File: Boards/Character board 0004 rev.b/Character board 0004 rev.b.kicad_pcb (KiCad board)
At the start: 2 copper layers, 166.4 x 186.7 mm, 65 parts, among them J1 card edge, J2 character connector, Q1 2N6125, U1 2.2K, U10 Unused DIP, U11 ULN2003A, U12 ULN2003A, U13 7406, U14 74LS42, U15 LM741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

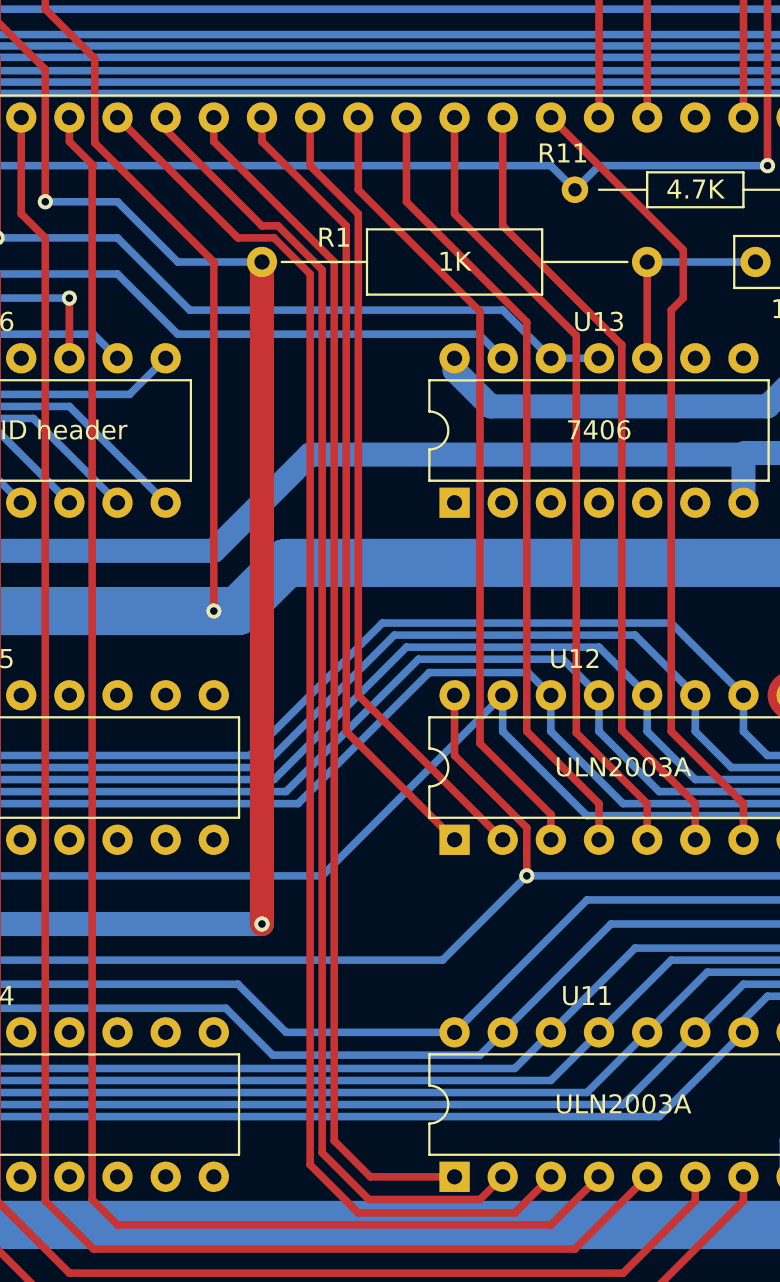
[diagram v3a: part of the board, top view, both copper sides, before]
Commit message: revisions from real life boards
tip130a is actually tip30a, widened holes for crystal, widened holes for big power resistor, fixed cpu board LED resistors
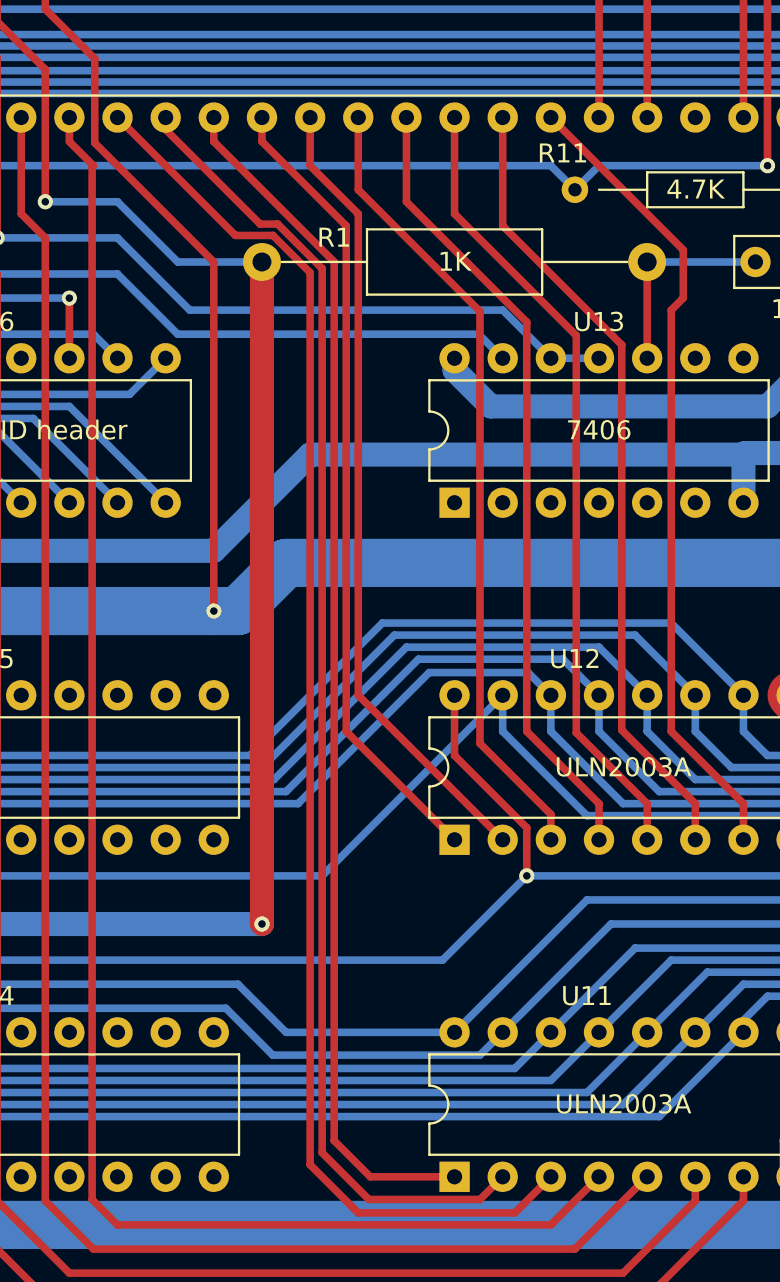
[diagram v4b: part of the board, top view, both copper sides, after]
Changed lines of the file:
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@@
     (fp_line (start 20.32 0) (end 14.66 0)
       (stroke (width 0.1) (type solid)) (layer "F.Fab"))
-    (pad "1" thru_hole circle (at 0 0) (size 1.6 1.6) (drill 0.8) (layers "*.Cu" "*.Mask")
+    (pad "1" thru_hole circle (at 0 0) (size 2 2) (drill 1) (layers "*.Cu" "*.Mask")
       (net 184 "24Vpu") (pintype "passive"))
-    (pad "2" thru_hole oval (at 20.32 0) (size 1.6 1.6) (drill 0.8) (layers "*.Cu" "*.Mask")
+    (pad "2" thru_hole circle (at 20.32 0) (size 2 2) (drill 1) (layers "*.Cu" "*.Mask")
       (net 182 "Net-(C11-Pad1)") (pintype "passive"))
     (model "${KICAD6_3DMODEL_DIR}/Resistor_THT.3dshapes/R_Axial_DIN0309_L9.0mm_D3.2mm_P20.32mm_Horizontal.wrl"
@@
   (segment (start 118.11 91.44) (end 118.04 91.51) (width 0.4) (layer "F.Cu") (net 170))
   (segment (start 116.84 90.17) (end 118.11 91.44) (width 0.4) (layer "F.Cu") (net 170))
-  (segment (start 119.38 88.9) (end 125.73 95.25) (width 0.4) (layer "F.Cu") (net 171))
-  (segment (start 125.73 95.25) (end 127.635 95.25) (width 0.4) (layer "F.Cu") (net 171))
-  (segment (start 132.08 146.685) (end 140.335 146.685) (width 0.4) (layer "F.Cu") (net 171))
+  (segment (start 127.579899 95.12) (end 129.54 97.080101) (width 0.4) (layer "F.Cu") (net 171))
+  (segment (start 119.38 88.9) (end 125.6 95.12) (width 0.4) (layer "F.Cu") (net 171))
+  (segment (start 129.54 97.080101) (end 129.54 144.145) (width 0.4) (layer "F.Cu") (net 171))
   (segment (start 140.335 146.685) (end 142.24 144.78) (width 0.4) (layer "F.Cu") (net 171))
+  (segment (start 132.08 146.685) (end 140.335 146.685) (width 0.4) (layer "F.Cu") (net 171))
   (segment (start 129.54 144.145) (end 132.08 146.685) (width 0.4) (layer "F.Cu") (net 171))
-  (segment (start 127.635 95.25) (end 129.54 97.155) (width 0.4) (layer "F.Cu") (net 171))
-  (segment (start 129.54 97.155) (end 129.54 144.145) (width 0.4) (layer "F.Cu") (net 171))
-  (segment (start 127.848528 94.615) (end 130.175 96.941472) (width 0.4) (layer "F.Cu") (net 172))
-  (segment (start 130.175 143.51) (end 132.645 145.98) (width 0.4) (layer "F.Cu") (net 172))
-  (segment (start 121.92 89.535) (end 127 94.615) (width 0.4) (layer "F.Cu") (net 172))
-  (segment (start 127 94.615) (end 127.848528 94.615) (width 0.4) (layer "F.Cu") (net 172))
-  (segment (start 130.175 96.941472) (end 130.175 143.51) (width 0.4) (layer "F.Cu") (net 172))
+  (segment (start 125.6 95.12) (end 127.579899 95.12) (width 0.4) (layer "F.Cu") (net 171))
+  (segment (start 132.645 145.98) (end 138.5 145.98) (width 0.4) (layer "F.Cu") (net 172))
+  (segment (start 126.905 94.52) (end 127.828427 94.52) (width 0.4) (layer "F.Cu") (net 172))
   (segment (start 121.92 88.9) (end 121.92 89.535) (width 0.4) (layer "F.Cu") (net 172))
+  (segment (start 130.175 96.866573) (end 130.175 143.51) (width 0.4) (layer "F.Cu") (net 172))
+  (segment (start 130.175 143.51) (end 132.645 145.98) (width 0.4) (layer "F.Cu") (net 172))
+  (segment (start 121.92 89.535) (end 126.905 94.52) (width 0.4) (layer "F.Cu") (net 172))
+  (segment (start 127.828427 94.52) (end 130.175 96.866573) (width 0.4) (layer "F.Cu") (net 172))
   (segment (start 138.5 145.98) (end 139.7 144.78) (width 0.4) (layer "F.Cu") (net 172))
-  (segment (start 132.645 145.98) (end 138.5 145.98) (width 0.4) (layer "F.Cu") (net 172))
-  (segment (start 124.46 90.17) (end 130.81 96.52) (width 0.4) (layer "F.Cu") (net 173))
+  (segment (start 130.81 142.875) (end 132.715 144.78) (width 0.4) (layer "F.Cu") (net 173))
+  (segment (start 132.715 144.78) (end 137.16 144.78) (width 0.4) (layer "F.Cu") (net 173))
   (segment (start 130.81 96.52) (end 130.81 142.875) (width 0.4) (layer "F.Cu") (net 173))
+  (segment (start 124.46 90.17) (end 130.81 96.52) (width 0.4) (layer "F.Cu") (net 173))
   (segment (start 124.46 88.9) (end 124.46 90.17) (width 0.4) (layer "F.Cu") (net 173))
-  (segment (start 132.715 144.78) (end 137.16 144.78) (width 0.4) (layer "F.Cu") (net 173))
-  (segment (start 130.81 142.875) (end 132.715 144.78) (width 0.4) (layer "F.Cu") (net 173))
   (segment (start 131.445 94.615) (end 131.445 121.285) (width 0.4) (layer "F.Cu") (net 174))
   (segment (start 127 88.9) (end 127 90.17) (width 0.4) (layer "F.Cu") (net 174))

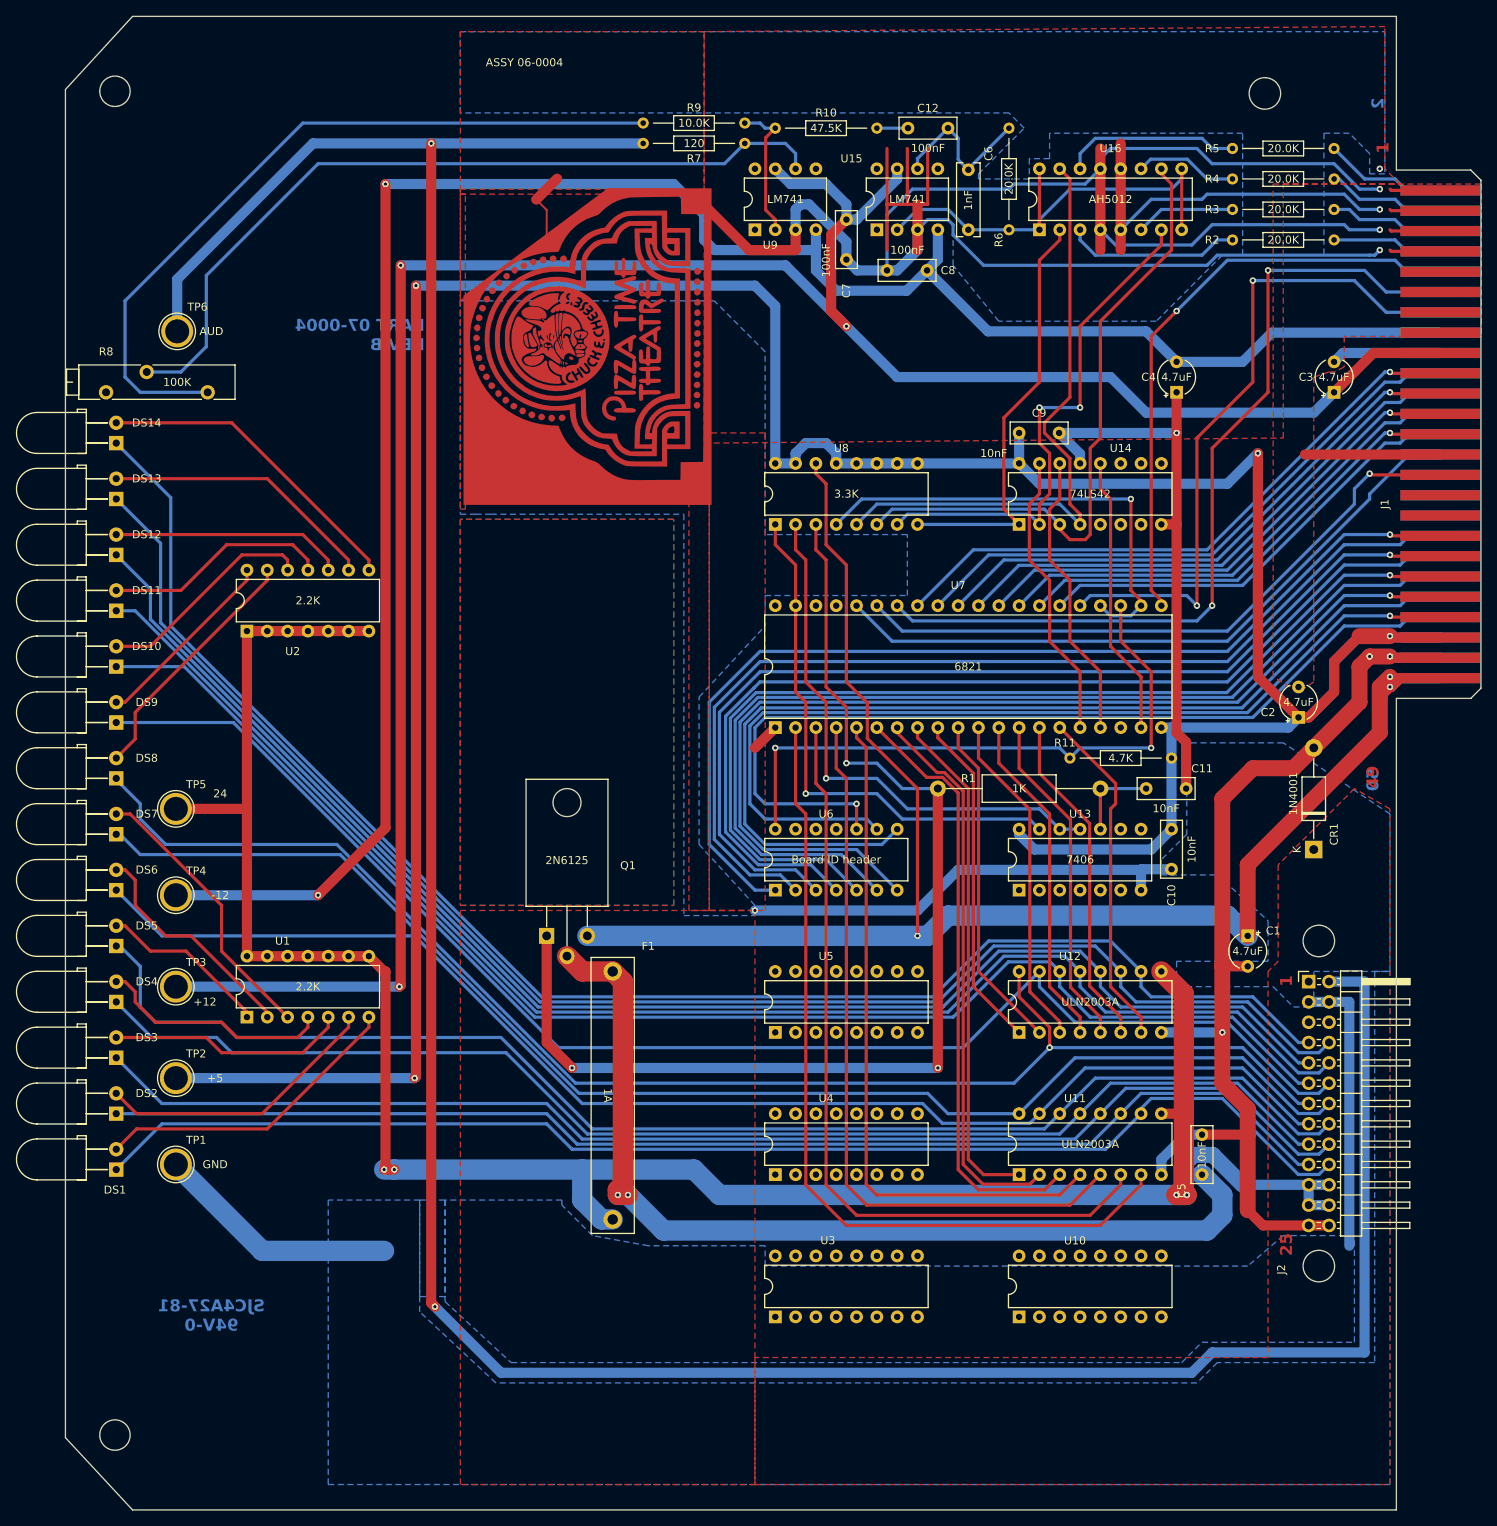
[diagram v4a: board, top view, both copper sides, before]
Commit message: revised PCBs based on Jen's boards, added rev.c
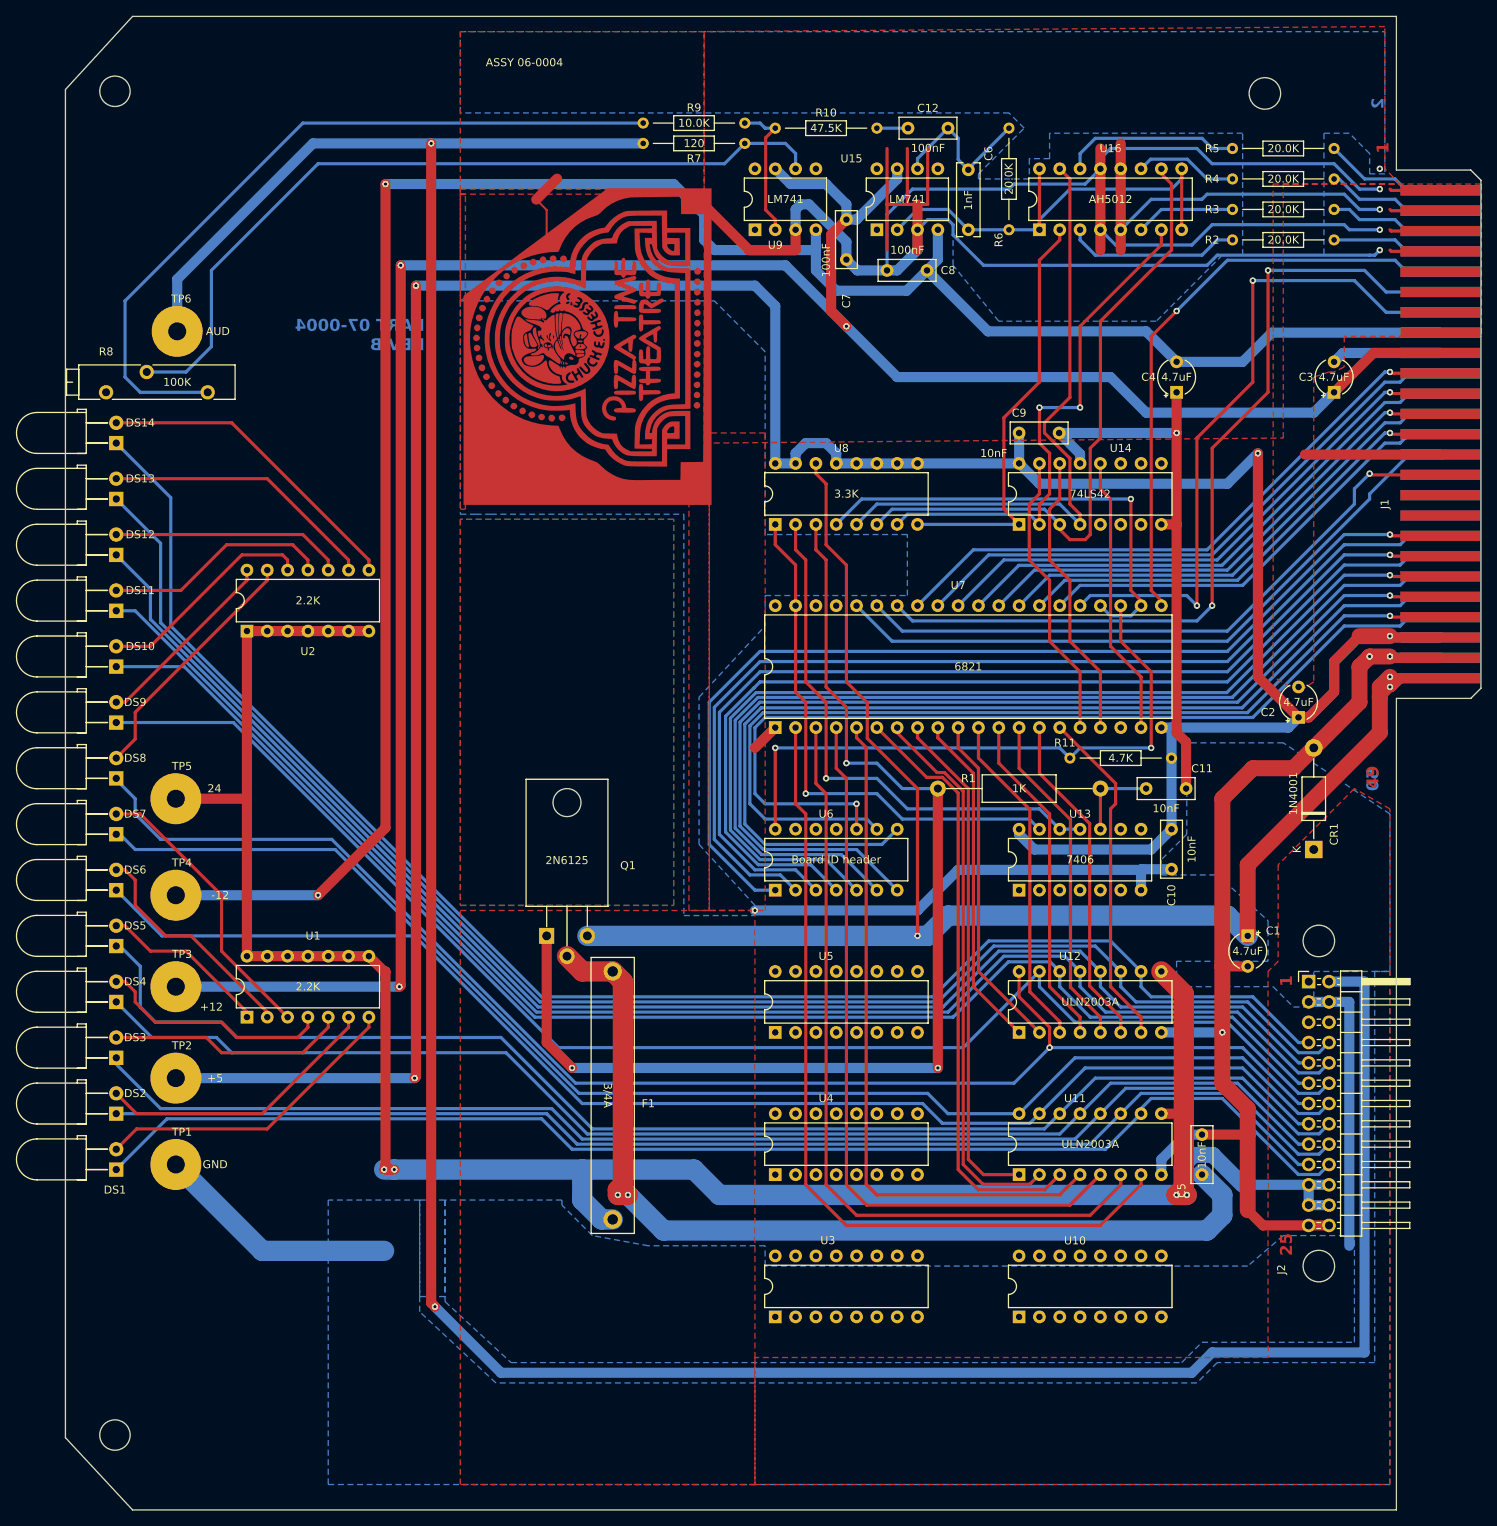
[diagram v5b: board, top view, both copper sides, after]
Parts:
- F1: value 1A -> 3/4A
- moved TP5 1.27 mm to (31.8, 97.8)
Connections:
- net BCLK renamed aux1_AGC
- net UNUSED1 renamed aux2_AGC
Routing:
- net Net-(DS7-A): track 35.3 -> 36.0 mm
- net A2out: track 162.4 -> 163.0 mm
- net A0out: track 162.7 -> 163.3 mm
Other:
- board text removed: "SJC4A27-81 94V-0"
